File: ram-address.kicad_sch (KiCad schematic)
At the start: 33 parts, among them SW3 SW_DIP_x08, U22 74HCT157, U23 74HCT157, U8 74HCT173, U9 74HCT173

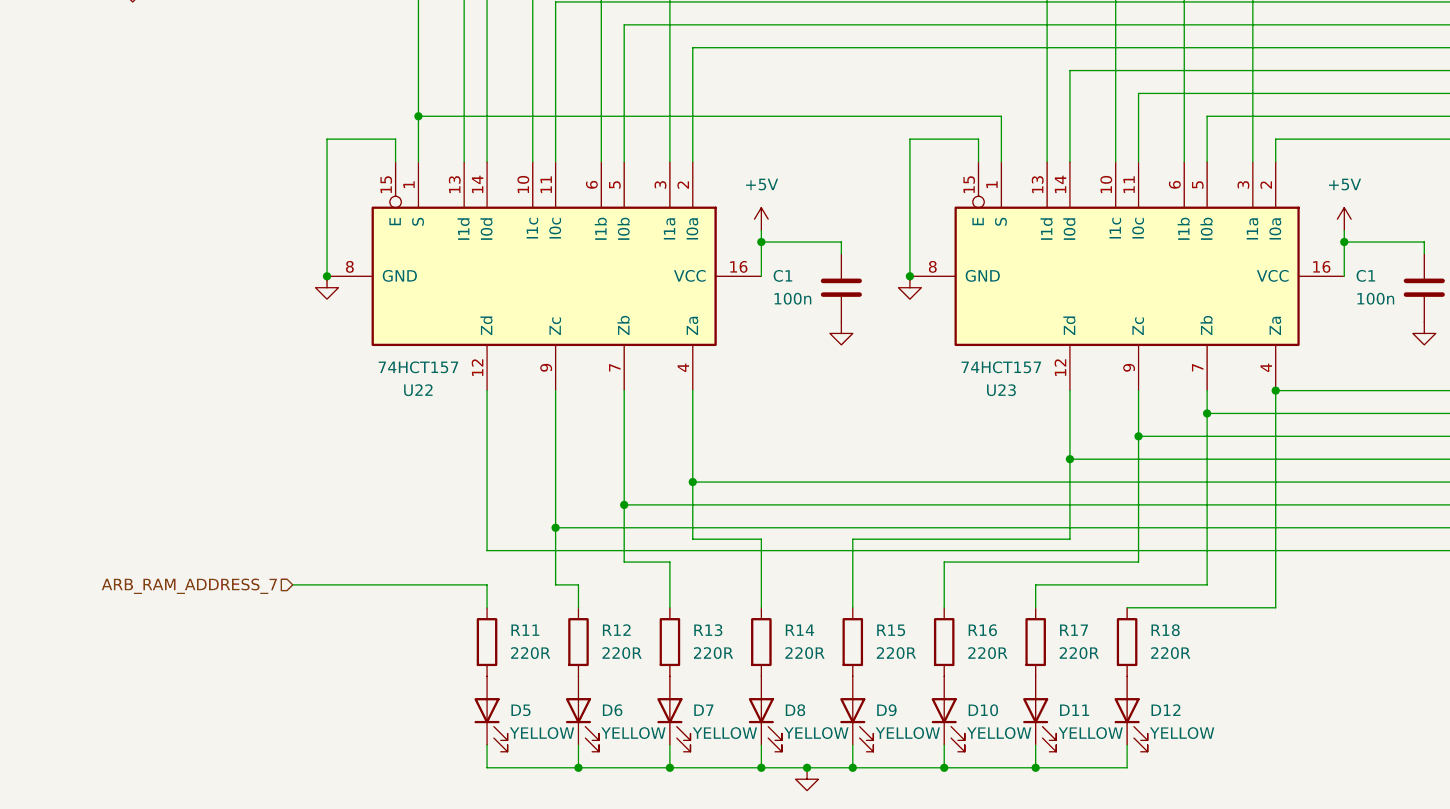
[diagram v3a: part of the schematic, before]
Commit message: changed symbols
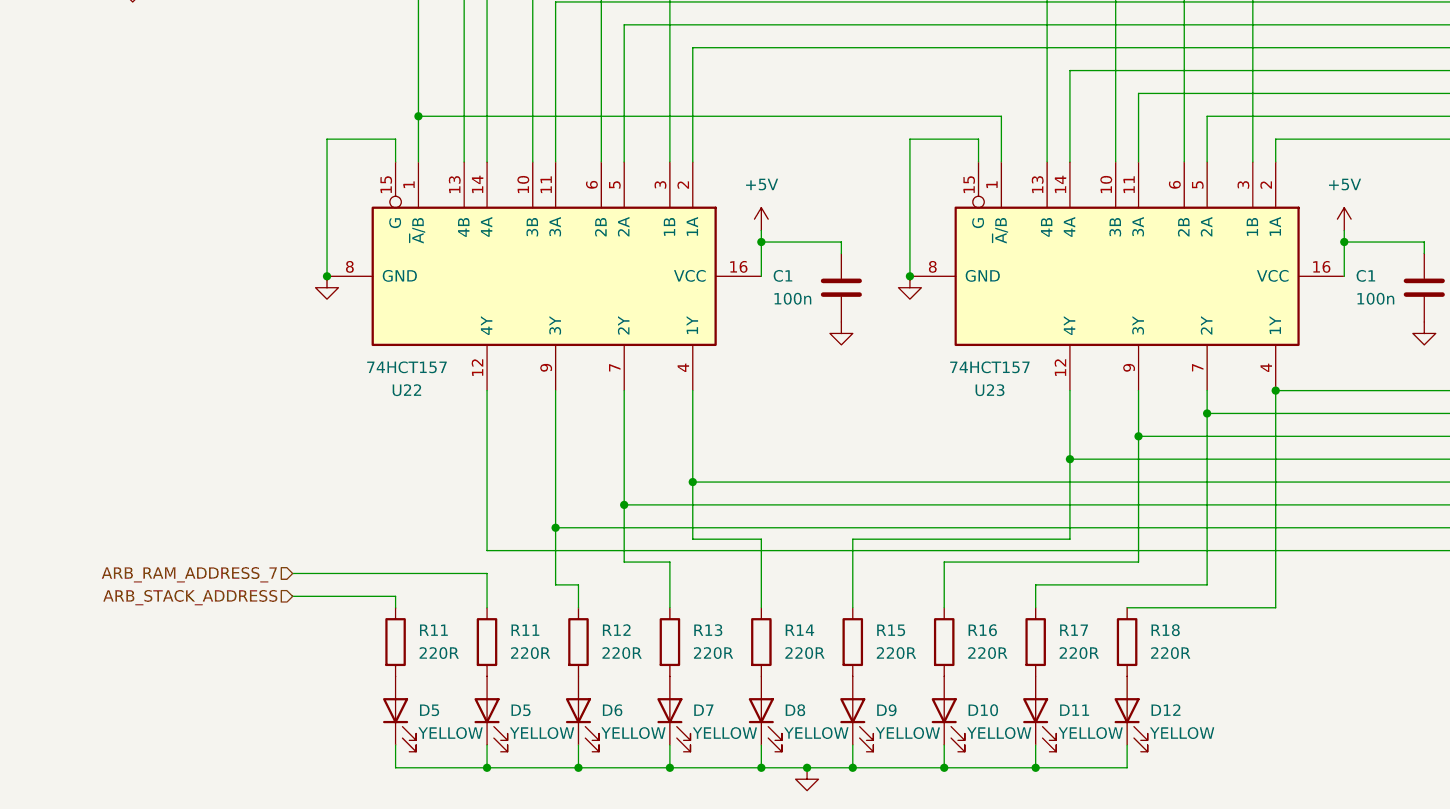
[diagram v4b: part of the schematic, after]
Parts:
- added D5: YELLOW, LED_THT:LED_D5.0mm, symbol Device:LED
- added R11: 220R, Resistor_THT:R_Axial_DIN0204_L3.6mm_D1.6mm_P7.62mm_Horizontal, symbol Device:R
- U22, U23: symbol 74xx:74LS157 -> 01_my_library:74HCT157
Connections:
- net GND: now also D5.1 (K)
- new net: D5.2 (A), R11.2
- new net ARB_STACK_ADDRESS: R11.1
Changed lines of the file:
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@@
   (junction (at 80.01 163.83) (diameter 0) (color 0 0 0 0)
   )
+  (junction (at 64.77 193.04) (diameter 0) (color 0 0 0 0)
+  )
   (junction (at 105.41 50.8) (diameter 0) (color 0 0 0 0)
   )
@@
     (stroke (width 0) (type default))
   )
-  (wire (pts (xy 64.77 172.72) (xy 64.77 175.26))
+  (wire (pts (xy 64.77 171.45) (xy 64.77 175.26))
     (stroke (width 0) (type default))
   )
@@
     (stroke (width 0) (type default))
   )
+  (wire (pts (xy 54.61 173.99) (xy 54.61 175.26))
+    (stroke (width 0) (type default))
+  )
   (wire (pts (xy 180.34 34.29) (xy 180.34 57.15))
     (stroke (width 0) (type default) (color 0 0 255 1))
@@
     (stroke (width 0) (type default))
   )
+  (wire (pts (xy 43.18 173.99) (xy 54.61 173.99))
+    (stroke (width 0) (type default))
+  )
   (wire (pts (xy 85.09 193.04) (xy 95.25 193.04))
     (stroke (width 0) (type default))
@@
     (stroke (width 0) (type default))
   )
-  (wire (pts (xy 43.18 172.72) (xy 64.77 172.72))
+  (wire (pts (xy 43.18 171.45) (xy 64.77 171.45))
     (stroke (width 0) (type default))
   )
@@
     (stroke (width 0) (type default))
   )
+  (wire (pts (xy 54.61 190.5) (xy 54.61 193.04))
+    (stroke (width 0) (type default))
+  )
   (wire (pts (xy 31.75 100.33) (xy 31.75 102.87))
     (stroke (width 0) (type default))
@@
   )
   (wire (pts (xy 261.62 134.62) (xy 177.8 134.62))
+    (stroke (width 0) (type default))
+  )
+  (wire (pts (xy 54.61 193.04) (xy 64.77 193.04))
     (stroke (width 0) (type default))
   )
@@
     (effects (font (size 1.27 1.27)) (justify left))
   )
+  (hierarchical_label "ARB_STACK_ADDRESS" (shape input) (at 43.18 173.99 180) (fields_autoplaced)
+    (effects (font (size 1.27 1.27)) (justify right))
+  )
   (hierarchical_label "RAM_ADDRESS_4" (shape output) (at 261.62 144.78 0) (fields_autoplaced)
     (effects (font (size 1.27 1.27)) (justify left))
@@
     (effects (font (size 1.27 1.27)) (justify left))
   )
-  (hierarchical_label "ARB_RAM_ADDRESS_7" (shape input) (at 43.18 172.72 180) (fields_autoplaced)
+  (hierarchical_label "ARB_RAM_ADDRESS_7" (shape input) (at 43.18 171.45 180) (fields_autoplaced)
     (effects (font (size 1.27 1.27)) (justify right))
   )
@@
     )
   )
-  (symbol (lib_id "74xx:74LS157") (at 137.16 138.43 270) (unit 1)
-    (in_bom yes) (on_board yes) (dnp no)
-    (property "Reference" "U23" (at 121.92 151.13 90)
+  (symbol (lib_id "01_my_library:74HCT157") (at 135.89 138.43 270) (unit 1)
+    (in_bom yes) (on_board yes) (dnp no)
+    (property "Reference" "U23" (at 120.65 151.13 90)
       (effects (font (size 1.27 1.27)))
     )
-    (property "Value" "74HCT157" (at 121.92 148.59 90)
+    (property "Value" "74HCT157" (at 120.65 148.59 90)
       (effects (font (size 1.27 1.27)))
     )
-    (property "Footprint" "Package_DIP:DIP-16_W7.62mm" (at 137.16 138.43 0)
-      (effects (font (size 1.27 1.27)) hide)
-    )
-    (property "Datasheet" "http://www.ti.com/lit/gpn/sn74LS157" (at 137.16 138.43 0)
+    (property "Footprint" "Package_DIP:DIP-16_W7.62mm" (at 135.89 139.7 0)
+      (effects (font (size 1.27 1.27)) hide)
+    )
+    (property "Datasheet" "https://www.ti.com/lit/ds/symlink/sn74hct157.pdf" (at 100.33 139.7 0)
       (effects (font (size 1.27 1.27)) hide)
     )
@@
     )
   )
+  (symbol (lib_id "Device:R") (at 54.61 179.07 0) (unit 1)
+    (in_bom yes) (on_board yes) (dnp no) (fields_autoplaced)
+    (property "Reference" "R11" (at 57.15 177.8 0)
+      (effects (font (size 1.27 1.27)) (justify left))
+    )
+    (property "Value" "220R" (at 57.15 180.34 0)
+      (effects (font (size 1.27 1.27)) (justify left))
+    )
+    (property "Footprint" "Resistor_THT:R_Axial_DIN0204_L3.6mm_D1.6mm_P7.62mm_Horizontal" (at 52.832 179.07 90)
+      (effects (font (size 1.27 1.27)) hide)
+    )
+    (property "Datasheet" "~" (at 54.61 179.07 0)
+      (effects (font (size 1.27 1.27)) hide)
+    )
+    (pin "2")
+    (pin "1")
+    (instances
+      (project "8-bit-cpu"
+        (path "/100bb8d1-c3d6-4e1f-87b6-72e4e187243c/651dfbaf-e340-4976-8216-793c5a5aaa3b"
+          (reference "R11") (unit 1)
+        )
+        (path "/100bb8d1-c3d6-4e1f-87b6-72e4e187243c/3568514a-e420-48fa-9fd5-7a290120765b"
+          (reference "R19") (unit 1)
+        )
+        (path "/100bb8d1-c3d6-4e1f-87b6-72e4e187243c/d6cd2240-d749-4685-b332-02e9e1af29c5"
+          (reference "R43") (unit 1)
+        )
+        (path "/100bb8d1-c3d6-4e1f-87b6-72e4e187243c/eeec1d6e-c04a-42fe-8103-cb8adc13344c"
+          (reference "R701") (unit 1)
+        )
+        (path "/100bb8d1-c3d6-4e1f-87b6-72e4e187243c/33b906b8-f63f-4a46-8ef2-4150917936b8/b8600875-f531-45d3-8c06-c8d636c0c136"
+          (reference "R167") (unit 1)
+        )
+      )
+    )
+  )
   (symbol (lib_id "power:GND") (at 46.99 138.43 0) (unit 1)
     (in_bom yes) (on_board yes) (dnp no) (fields_autoplaced)
@@
         (path "/100bb8d1-c3d6-4e1f-87b6-72e4e187243c/33b906b8-f63f-4a46-8ef2-4150917936b8/b8600875-f531-45d3-8c06-c8d636c0c136"
           (reference "#PWR090") (unit 1)
+        )
+      )
+    )
+  )
+  (symbol (lib_id "Device:LED") (at 54.61 186.69 90) (unit 1)
+    (in_bom yes) (on_board yes) (dnp no)
+    (property "Reference" "D5" (at 57.15 186.69 90)
+      (effects (font (size 1.27 1.27)) (justify right))
+    )
+    (property "Value" "YELLOW" (at 57.15 189.23 90)
+      (effects (font (size 1.27 1.27)) (justify right))
+    )
+    (property "Footprint" "LED_THT:LED_D5.0mm" (at 54.61 186.69 0)
+      (effects (font (size 1.27 1.27)) hide)
+    )
+    (property "Datasheet" "~" (at 54.61 186.69 0)
+      (effects (font (size 1.27 1.27)) hide)
+    )
+    (pin "1")
+    (pin "2")
+    (instances
+      (project "8-bit-cpu"
+        (path "/100bb8d1-c3d6-4e1f-87b6-72e4e187243c/651dfbaf-e340-4976-8216-793c5a5aaa3b"
+          (reference "D5") (unit 1)
+        )
+        (path "/100bb8d1-c3d6-4e1f-87b6-72e4e187243c/3568514a-e420-48fa-9fd5-7a290120765b"
+          (reference "D13") (unit 1)
+        )
+        (path "/100bb8d1-c3d6-4e1f-87b6-72e4e187243c/d6cd2240-d749-4685-b332-02e9e1af29c5"
+          (reference "D29") (unit 1)
+        )
+        (path "/100bb8d1-c3d6-4e1f-87b6-72e4e187243c/eeec1d6e-c04a-42fe-8103-cb8adc13344c"
+          (reference "D701") (unit 1)
+        )
+        (path "/100bb8d1-c3d6-4e1f-87b6-72e4e187243c/33b906b8-f63f-4a46-8ef2-4150917936b8/b8600875-f531-45d3-8c06-c8d636c0c136"
+          (reference "D123") (unit 1)
         )
       )
@@
     )
   )
-  (symbol (lib_id "74xx:74LS157") (at 72.39 138.43 270) (unit 1)
-    (in_bom yes) (on_board yes) (dnp no)
-    (property "Reference" "U22" (at 57.15 151.13 90)
+  (symbol (lib_id "01_my_library:74HCT157") (at 71.12 138.43 270) (unit 1)
+    (in_bom yes) (on_board yes) (dnp no)
+    (property "Reference" "U22" (at 55.88 151.13 90)
       (effects (font (size 1.27 1.27)))
     )
-    (property "Value" "74HCT157" (at 57.15 148.59 90)
+    (property "Value" "74HCT157" (at 55.88 148.59 90)
       (effects (font (size 1.27 1.27)))
     )
-    (property "Footprint" "Package_DIP:DIP-16_W7.62mm" (at 72.39 138.43 0)
-      (effects (font (size 1.27 1.27)) hide)
-    )
-    (property "Datasheet" "http://www.ti.com/lit/gpn/sn74LS157" (at 72.39 138.43 0)
-      (effects (font (size 1.27 1.27)) hide)
-    )
+    (property "Footprint" "Package_DIP:DIP-16_W7.62mm" (at 71.12 139.7 0)
+      (effects (font (size 1.27 1.27)) hide)
+    )
+    (property "Datasheet" "https://www.ti.com/lit/ds/symlink/sn74hct157.pdf" (at 35.56 139.7 0)
+      (effects (font (size 1.27 1.27)) hide)
+    )
